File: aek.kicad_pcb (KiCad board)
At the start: 2 copper layers, 437.9 x 141 mm, 225 parts, among them J1 Conn_01x04_MountingPin, SW1 SW_Push, U1 ATmega32U4-AU, Y1 16MHz

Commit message: reposition mcu
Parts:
- moved C3 25.1 mm to (421.1, 39.2)
- moved C4 25.1 mm to (428.3, 37.5)
- moved C5 25.1 mm to (414.0, 32.4)
- moved C6 25.1 mm to (435.7, 26.9)
- moved R3 25.1 mm to (434.1, 40.8)
- moved R4 25.1 mm to (414.0, 22.1)
- moved SW1 25.1 mm to (428.4, 43.5)
- moved C1 25.1 mm to (418.6, 19.0)
- moved C2 25.1 mm to (411.7, 32.4)
- moved C7 25.1 mm to (431.2, 37.5)
- moved U1 25.1 mm to (423.6, 27.8)
- moved Y1 25.1 mm to (424.1, 37.3)
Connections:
- U1 pad 36: ROW9 -> ROW10
- U1 pad 38: ROW10 -> ROW9
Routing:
- net COL4: track 436.4 -> 463.3 mm
- net COL6: track 389.4 -> 416.2 mm
- net COL2: track 539.0 -> 565.6 mm
- net COL1: track 565.2 -> 591.7 mm
- net ROW9: track 559.0 -> 585.5 mm, vias 8 -> 6
- net COL3: track 460.1 -> 486.3 mm
- net COL0: track 617.7 -> 643.9 mm
- net COL7: track 311.0 -> 337.1 mm
- net COL5: track 403.5 -> 429.4 mm
- net COL8: track 307.4 -> 333.1 mm
- net ROW4: track 571.3 -> 596.6 mm
- net D-: track 46.8 -> 21.6 mm
- net D+: track 47.9 -> 22.7 mm
- net ROW0: track 485.2 -> 510.4 mm, vias 0 -> 2
- net +5V: track 76.9 -> 51.8 mm
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
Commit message: cleanup
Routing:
- net COL8: track 333.1 -> 326.9 mm
- net ROW1: track 502.8 -> 500.3 mm
- net ROW10: track 599.4 -> 597.6 mm
- net ROW9: track 585.5 -> 583.8 mm
- net COL2: track 565.6 -> 565.1 mm
- net ROW5: track 571.2 -> 571.7 mm

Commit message: cleanup
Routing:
- net ROW10: track 597.6 -> 588.8 mm
- net ROW5: track 571.7 -> 567.6 mm
- net COL8: track 326.9 -> 330.9 mm
- net ROW1: track 500.3 -> 496.5 mm
- net ROW6: track 688.9 -> 685.4 mm
- net ROW4: track 596.2 -> 592.7 mm
- net ROW8: track 626.8 -> 623.4 mm
- net ROW2: track 516.1 -> 512.9 mm
- net ROW0: track 510.4 -> 513.4 mm
- net ROW7: track 599.0 -> 596.1 mm
- net ROW3: track 615.4 -> 612.8 mm

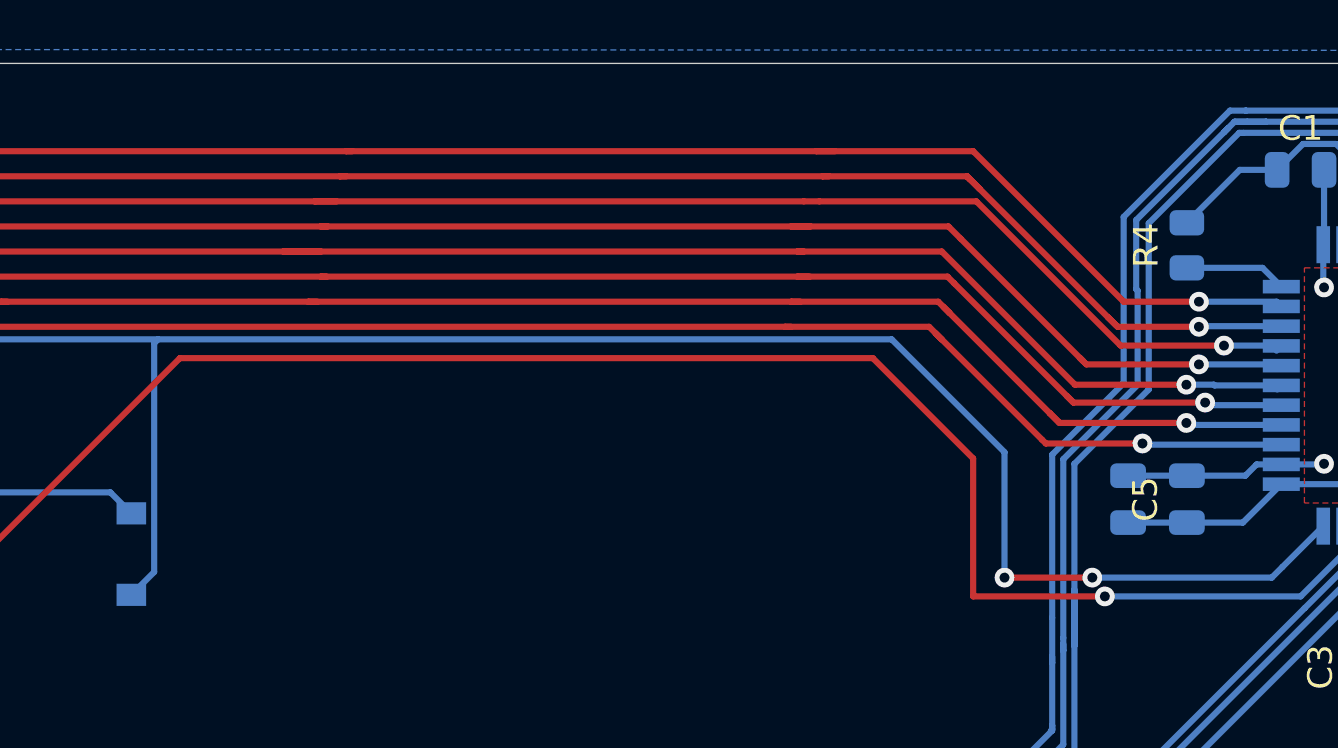
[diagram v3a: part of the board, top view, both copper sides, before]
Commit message: make more space for leds
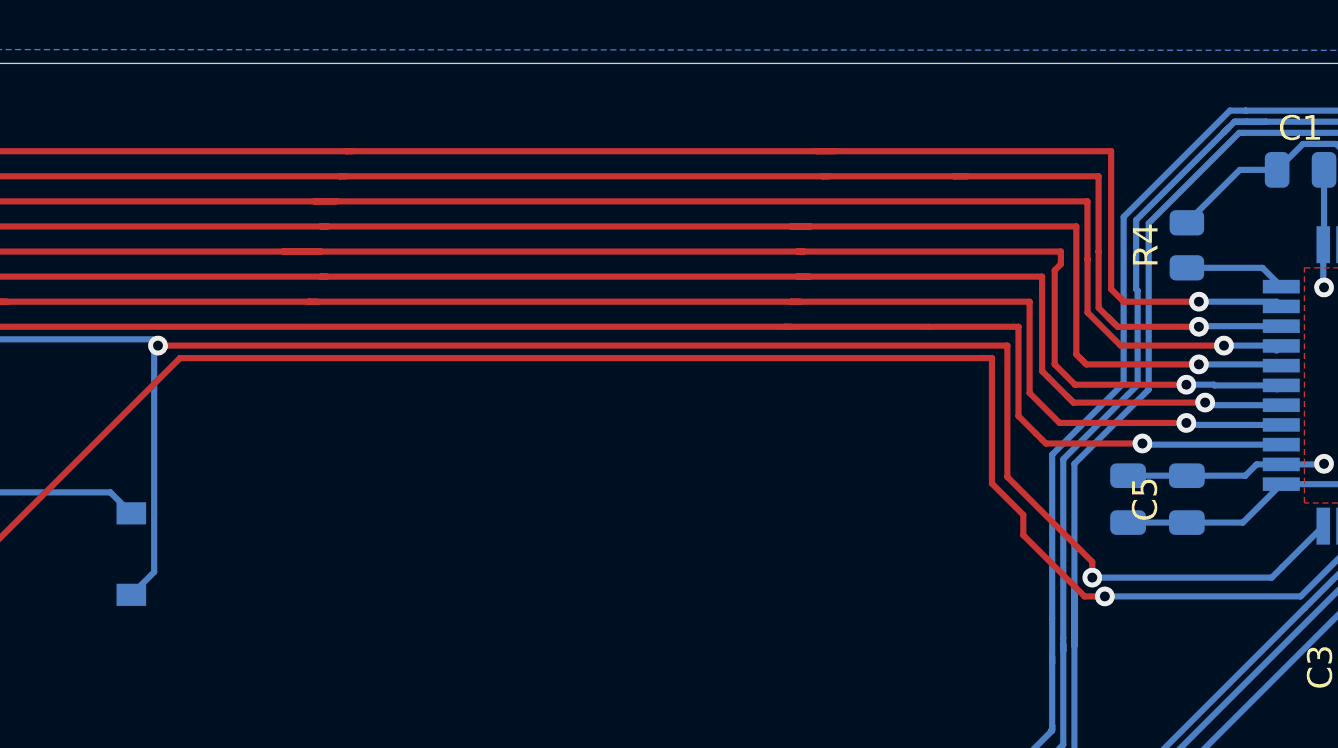
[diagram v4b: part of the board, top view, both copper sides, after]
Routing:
- net COL0: track 643.9 -> 647.1 mm
- net COL4: track 463.4 -> 466.4 mm
- net COL3: track 486.5 -> 489.6 mm
- net COL1: track 592.2 -> 594.9 mm
- net COL2: track 565.1 -> 567.7 mm
- net COL5: track 429.7 -> 432.0 mm
- net COL7: track 336.8 -> 338.6 mm
- net COL6: track 416.2 -> 417.5 mm

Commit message: fix
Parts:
- moved C4 14.7 mm to (430.6, 51.9)
- moved C6 14.7 mm to (438.0, 41.4)
- moved C7 14.7 mm to (433.5, 51.9)
- moved R3 14.7 mm to (436.4, 55.3)
- moved SW1 14.7 mm to (430.7, 58.0)
- moved U1 14.7 mm to (425.9, 42.3)
- moved Y1 14.7 mm to (426.3, 51.8)
- moved C1 14.7 mm to (420.9, 33.5)
- moved R4 14.7 mm to (416.3, 36.6)
- moved C2 14.7 mm to (413.9, 46.9)
- moved C3 14.7 mm to (423.4, 53.7)
- moved C5 14.7 mm to (416.3, 46.9)
- turned D100 to 0 degrees
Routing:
- net COL2: track 567.7 -> 585.9 mm
- net COL6: track 417.5 -> 435.0 mm
- net COL1: track 594.9 -> 612.5 mm
- net COL8: track 331.1 -> 348.3 mm
- net COL5: track 432.0 -> 449.3 mm
- net COL4: track 466.4 -> 483.6 mm
- net COL0: track 647.1 -> 664.2 mm
- net COL7: track 338.6 -> 355.5 mm
- net COL3: track 489.6 -> 506.4 mm
- net ROW0: track 513.5 -> 530.2 mm
- net D-: track 21.6 -> 11.9 mm
- net D+: track 22.7 -> 13.2 mm
- net +5V: track 51.8 -> 42.7 mm
- net ROW10: track 588.8 -> 581.3 mm, vias 0 -> 4
- net ROW6: track 685.4 -> 678.1 mm
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
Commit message: updates
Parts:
- added C10: 0.1uF, Capacitor_SMD:C_0805_2012Metric, F.Cu at (433.9, 28.0)
- added C8: 0.1uF, Capacitor_SMD:C_0805_2012Metric, F.Cu at (412.0, 28.0)
- added C9: 0.1uF, Capacitor_SMD:C_0805_2012Metric, F.Cu at (392.0, 28.0)
- added LED1: WS2812B, LED_SMD:LED_WS2812B_PLCC4_5.0x5.0mm_P3.2mm, F.Cu at (384.9, 28.0)
- added LED2: WS2812B, LED_SMD:LED_WS2812B_PLCC4_5.0x5.0mm_P3.2mm, F.Cu at (404.9, 28.0)
- added LED3: WS2812B, LED_SMD:LED_WS2812B_PLCC4_5.0x5.0mm_P3.2mm, F.Cu at (424.9, 28.0)
- added R1: 330, Resistor_SMD:R_0805_2012Metric, F.Cu at (428.8, 32.9)
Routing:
- net VCC: track 0.00 -> 91.1 mm, vias 0 -> 1
- net GND: track 173.9 -> 200.0 mm, vias 55 -> 59
- net Net-(LED2-Pad4): track 0.00 -> 23.0 mm
- net ROW9: track 589.6 -> 568.2 mm, vias 8 -> 7
- net COL8: track 348.3 -> 327.0 mm
- net ROW0: track 530.2 -> 512.4 mm
- net Net-(LED1-Pad4): track 0.00 -> 17.1 mm
- net D-: track 11.9 -> 28.4 mm
- net D+: track 13.2 -> 29.6 mm
- net +5V: track 42.7 -> 58.9 mm
- net COL4: track 483.6 -> 470.2 mm
- net COL2: track 585.9 -> 572.9 mm
- net COL0: track 664.2 -> 651.7 mm
- net COL3: track 506.4 -> 494.1 mm
- net COL5: track 449.3 -> 437.5 mm
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
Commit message: updates
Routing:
- net GND: track 200.0 -> 221.0 mm, vias 59 -> 72
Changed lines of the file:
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@@
     (thickness 1.6)
     (drawings 15)
-    (tracks 1659)
+    (tracks 1678)
     (zones 0)
     (modules 232)
@@
   (segment (start 422.727001 37.628251) (end 427.445749 37.628251) (width 0.25) (layer B.Cu) (net 1))
   (segment (start 427.445749 37.628251) (end 428.976999 37.628251) (width 0.25) (layer B.Cu) (net 1))
+  (via (at 447.04 49.276) (size 0.8) (drill 0.4) (layers F.Cu B.Cu) (net 1))
+  (via (at 442.722 49.276) (size 0.8) (drill 0.4) (layers F.Cu B.Cu) (net 1))
+  (segment (start 447.04 49.276) (end 442.722 49.276) (width 0.25) (layer F.Cu) (net 1))
+  (via (at 408.94 52.07) (size 0.8) (drill 0.4) (layers F.Cu B.Cu) (net 1))
+  (via (at 413.512 52.07) (size 0.8) (drill 0.4) (layers F.Cu B.Cu) (net 1))
+  (segment (start 408.94 52.07) (end 413.512 52.07) (width 0.25) (layer F.Cu) (net 1))
+  (via (at 407.67 83.82) (size 0.8) (drill 0.4) (layers F.Cu B.Cu) (net 1))
+  (via (at 407.67 80.772) (size 0.8) (drill 0.4) (layers F.Cu B.Cu) (net 1))
+  (segment (start 407.67 83.82) (end 407.67 80.772) (width 0.25) (layer F.Cu) (net 1))
+  (via (at 385.318 115.824) (size 0.8) (drill 0.4) (layers F.Cu B.Cu) (net 1))
+  (via (at 387.604 118.11) (size 0.8) (drill 0.4) (layers F.Cu B.Cu) (net 1))
+  (segment (start 385.318 115.824) (end 387.604 118.11) (width 0.25) (layer F.Cu) (net 1))
+  (via (at 398.018 64.77) (size 0.8) (drill 0.4) (layers F.Cu B.Cu) (net 1))
+  (via (at 398.018 64.77) (size 0.8) (drill 0.4) (layers F.Cu B.Cu) (net 1))
+  (via (at 398.018 67.31) (size 0.8) (drill 0.4) (layers F.Cu B.Cu) (net 1))
+  (segment (start 398.018 64.77) (end 398.018 67.31) (width 0.25) (layer F.Cu) (net 1))
+  (via (at 424.688 77.216) (size 0.8) (drill 0.4) (layers F.Cu B.Cu) (net 1))
+  (via (at 424.688 73.914) (size 0.8) (drill 0.4) (layers F.Cu B.Cu) (net 1))
+  (segment (start 424.688 77.216) (end 424.688 73.914) (width 0.25) (layer F.Cu) (net 1))
   (segment (start 429.82075 36.5845) (end 429.852 36.55325) (width 0.25) (layer B.Cu) (net 2) (status 30))
   (segment (start 428.252 47.95325) (end 428.252 48.95325) (width 0.25) (layer B.Cu) (net 2) (status 10))

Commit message: update
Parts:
- moved C3 0.81 mm to (422.9, 54.3)
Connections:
- C10 pad 2: VCC -> +5V
- C8 pad 2: VCC -> +5V
- C9 pad 2: VCC -> +5V
- LED1 pad 1: VCC -> +5V
- LED2 pad 1: VCC -> +5V
- LED3 pad 1: VCC -> +5V
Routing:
- net VCC: track 91.1 -> 0.00 mm, vias 1 -> 0
- net +5V: track 58.9 -> 147.6 mm, vias 5 -> 6
- net ROW2: track 514.0 -> 509.7 mm
- net GND: track 221.0 -> 217.3 mm
- net Net-(C3-Pad1): track 6.46 -> 7.30 mm
